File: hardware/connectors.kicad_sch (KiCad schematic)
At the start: 16 parts, among them J2 USB_C_Receptacle_USB2.0_16P, J7 Barrel_Jack_Switch

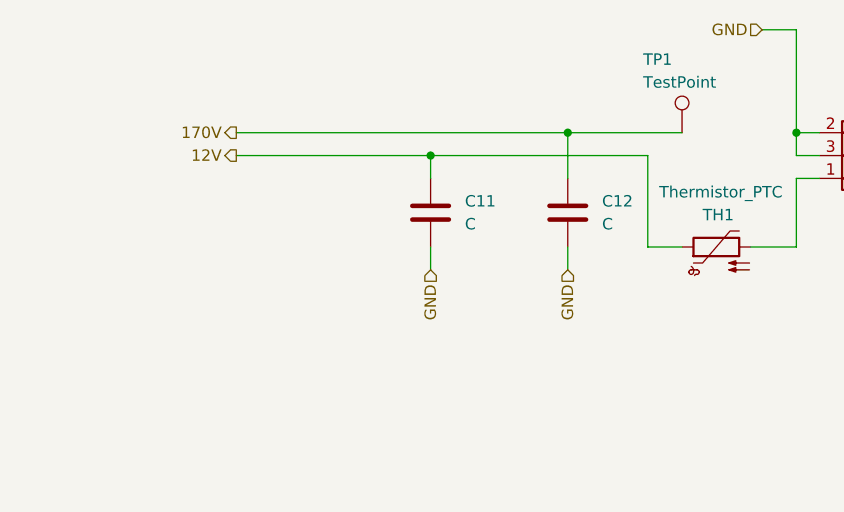
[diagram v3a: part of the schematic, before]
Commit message: Rework HT PSU placement.
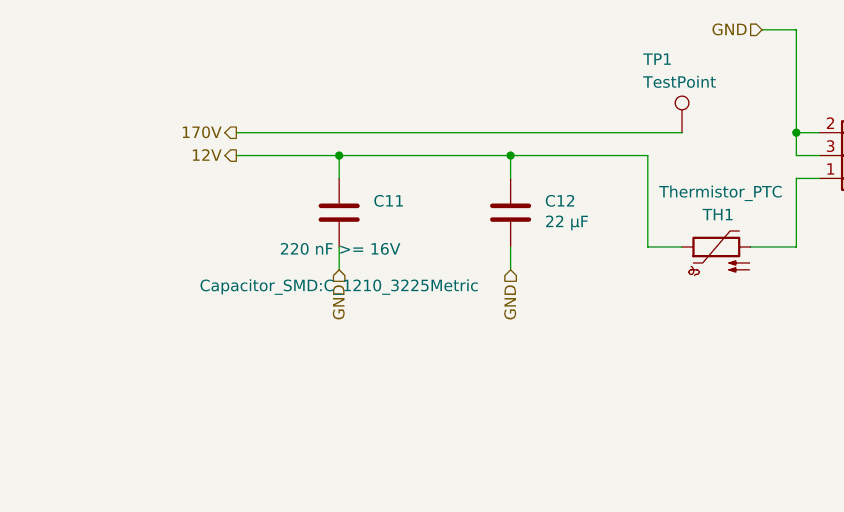
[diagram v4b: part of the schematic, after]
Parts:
- C11: value C -> 220 nF >= 16V; footprint Capacitor_SMD:C_1206_3216Metric -> Capacitor_SMD:C_1210_3225Metric
- C12: value C -> 22 µF; footprint Capacitor_THT:CP_Radial_D8.0mm_P3.50mm -> Capacitor_SMD:CP_Elec_6.3x5.4
- TP1: footprint TestPoint:TestPoint_Pad_D2.0mm -> TestPoint:TestPoint_Pad_D1.5mm
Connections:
- net 12V: now also C12.1
- net 170V: no longer C12.1
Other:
- moved on the sheet: C11
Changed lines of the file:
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@@
-	)
-	(junction
-		(at 189.23 38.1)
-		(diameter 0)
-		(color 0 0 0 0)
 	)
 	(junction
@@
 	)
 	(junction
-		(at 173.99 40.64)
+		(at 182.88 40.64)
 		(diameter 0)
 		(color 0 0 0 0)
 	)
-	(wire
-		(pts
-			(xy 173.99 43.18) (xy 173.99 40.64)
+	(junction
+		(at 163.83 40.64)
+		(diameter 0)
+		(color 0 0 0 0)
+	)
+	(wire
+		(pts
+			(xy 163.83 43.18) (xy 163.83 40.64)
 		)
 		(stroke
@@
 	(wire
 		(pts
+			(xy 182.88 50.8) (xy 182.88 53.34)
+		)
+		(stroke
+			(width 0)
+			(type default)
+		)
+	)
+	(wire
+		(pts
 			(xy 198.12 50.8) (xy 201.93 50.8)
 		)
@@
 	(wire
 		(pts
-			(xy 189.23 50.8) (xy 189.23 53.34)
-		)
-		(stroke
-			(width 0)
-			(type default)
-		)
-	)
-	(wire
-		(pts
 			(xy 105.41 52.07) (xy 111.76 52.07)
 		)
@@
 	(wire
 		(pts
+			(xy 182.88 43.18) (xy 182.88 40.64)
+		)
+		(stroke
+			(width 0)
+			(type default)
+		)
+	)
+	(wire
+		(pts
 			(xy 77.47 57.15) (xy 83.82 57.15)
 		)
@@
 	(wire
 		(pts
-			(xy 189.23 38.1) (xy 189.23 43.18)
+			(xy 182.88 40.64) (xy 198.12 40.64)
 		)
 		(stroke
@@
 	(wire
 		(pts
-			(xy 173.99 53.34) (xy 173.99 50.8)
-		)
-		(stroke
-			(width 0)
-			(type default)
-		)
-	)
-	(wire
-		(pts
 			(xy 60.96 82.55) (xy 60.96 96.52)
 		)
@@
 	(wire
 		(pts
-			(xy 189.23 38.1) (xy 201.93 38.1)
-		)
-		(stroke
-			(width 0)
-			(type default)
-		)
-	)
-	(wire
-		(pts
 			(xy 209.55 50.8) (xy 214.63 50.8)
 		)
@@
 	(wire
 		(pts
-			(xy 152.4 40.64) (xy 173.99 40.64)
-		)
-		(stroke
-			(width 0)
-			(type default)
-		)
-	)
-	(wire
-		(pts
-			(xy 152.4 38.1) (xy 189.23 38.1)
+			(xy 152.4 40.64) (xy 163.83 40.64)
+		)
+		(stroke
+			(width 0)
+			(type default)
+		)
+	)
+	(wire
+		(pts
+			(xy 152.4 38.1) (xy 201.93 38.1)
 		)
 		(stroke
@@
 	(wire
 		(pts
+			(xy 163.83 50.8) (xy 163.83 53.34)
+		)
+		(stroke
+			(width 0)
+			(type default)
+		)
+	)
+	(wire
+		(pts
 			(xy 76.2 74.93) (xy 78.74 74.93)
 		)
@@
 	(wire
 		(pts
-			(xy 173.99 40.64) (xy 198.12 40.64)
-		)
-		(stroke
-			(width 0)
-			(type default)
-		)
-	)
-	(wire
-		(pts
 			(xy 214.63 38.1) (xy 217.17 38.1)
 		)
@@
 		(pts
 			(xy 53.34 92.71) (xy 53.34 96.52)
+		)
+		(stroke
+			(width 0)
+			(type default)
+		)
+	)
+	(wire
+		(pts
+			(xy 163.83 40.64) (xy 182.88 40.64)
 		)
 		(stroke
@@
 		)
 	)
+	(hierarchical_label "GND"
+		(shape input)
+		(at 182.88 53.34 270)
+		(effects
+			(font
+				(size 1.27 1.27)
+			)
+			(justify right)
+		)
+	)
 	(hierarchical_label "D+"
 		(shape output)
@@
 	(hierarchical_label "GND"
 		(shape input)
-		(at 173.99 53.34 270)
-		(effects
-			(font
-				(size 1.27 1.27)
-			)
-			(justify right)
-		)
-	)
-	(hierarchical_label "GND"
-		(shape input)
-		(at 189.23 53.34 270)
+		(at 163.83 53.34 270)
 		(effects
 			(font
@@
 	(symbol
 		(lib_id "Device:C")
-		(at 173.99 46.99 0)
+		(at 182.88 46.99 0)
 		(unit 1)
 		(exclude_from_sim no)
@@
 		(on_board yes)
 		(dnp no)
-		(fields_autoplaced yes)
+		(property "Reference" "C12"
+			(at 186.69 45.7199 0)
+			(effects
+				(font
+					(size 1.27 1.27)
+				)
+				(justify left)
+			)
+		)
+		(property "Value" "22 µF"
+			(at 186.69 48.006 0)
+			(effects
+				(font
+					(size 1.27 1.27)
+				)
+				(justify left)
+			)
+		)
+		(property "Footprint" "Capacitor_SMD:CP_Elec_6.3x5.4"
+			(at 183.8452 50.8 0)
+			(effects
+				(font
+					(size 1.27 1.27)
+				)
+				(hide yes)
+			)
+		)
+		(property "Datasheet" "~"
+			(at 182.88 46.99 0)
+			(effects
+				(font
+					(size 1.27 1.27)
+				)
+				(hide yes)
+			)
+		)
+		(property "Description" "Unpolarized capacitor"
+			(at 182.88 46.99 0)
+			(effects
+				(font
+					(size 1.27 1.27)
+				)
+				(hide yes)
+			)
+		)
+		(pin "1"
+		)
+		(pin "2"
+		)
+		(instances
+			(project "nixie_clock"
+				(path "/90430e5f-7049-4de8-b92d-f897c4a89819/7e2fbc03-0d09-4c94-a49f-ff5156ee2f2b"
+					(reference "C12")
+					(unit 1)
+				)
+			)
+		)
+	)
+	(symbol
+		(lib_id "Device:C")
+		(at 163.83 46.99 0)
+		(unit 1)
+		(exclude_from_sim no)
+		(in_bom yes)
+		(on_board yes)
+		(dnp no)
 		(property "Reference" "C11"
-			(at 177.8 45.7199 0)
-			(effects
-				(font
-					(size 1.27 1.27)
-				)
-				(justify left)
-			)
-		)
-		(property "Value" "C"
-			(at 177.8 48.2599 0)
-			(effects
-				(font
-					(size 1.27 1.27)
-				)
-				(justify left)
-			)
-		)
-		(property "Footprint" "Capacitor_SMD:C_1206_3216Metric"
-			(at 174.9552 50.8 0)
-			(effects
-				(font
-					(size 1.27 1.27)
-				)
-				(hide yes)
+			(at 167.64 45.7199 0)
+			(effects
+				(font
+					(size 1.27 1.27)
+				)
+				(justify left)
+			)
+		)
+		(property "Value" "220 nF >= 16V"
+			(at 157.226 51.054 0)
+			(effects
+				(font
+					(size 1.27 1.27)
+				)
+				(justify left)
+			)
+		)
+		(property "Footprint" "Capacitor_SMD:C_1210_3225Metric"
+			(at 163.83 55.118 0)
+			(effects
+				(font
+					(size 1.27 1.27)
+				)
 			)
 		)
 		(property "Datasheet" "~"
-			(at 173.99 46.99 0)
+			(at 163.83 46.99 0)
 			(effects
 				(font
@@
 		)
 		(property "Description" "Unpolarized capacitor"
-			(at 173.99 46.99 0)
+			(at 163.83 46.99 0)
 			(effects
 				(font
@@
 			)
 		)
-		(property "Footprint" "TestPoint:TestPoint_Pad_D2.0mm"
+		(property "Footprint" "TestPoint:TestPoint_Pad_D1.5mm"
 			(at 207.01 38.1 0)
 			(effects
@@
 					(unit 1)
 				)
-			)
-		)
-	)
-	(symbol
-		(lib_id "Device:C")
-		(at 189.23 46.99 0)
-		(unit 1)
-		(exclude_from_sim no)
-		(in_bom yes)
-		(on_board yes)
-		(dnp no)
-		(fields_autoplaced yes)
-		(property "Reference" "C12"
-			(at 193.04 45.7199 0)
-			(effects
-				(font
-					(size 1.27 1.27)
-				)
-				(justify left)
-			)
-		)
-		(property "Value" "C"
-			(at 193.04 48.2599 0)
-			(effects
-				(font
-					(size 1.27 1.27)
-				)
-				(justify left)
-			)
-		)
-		(property "Footprint" "Capacitor_THT:CP_Radial_D8.0mm_P3.50mm"
-			(at 190.1952 50.8 0)
-			(effects
-				(font
-					(size 1.27 1.27)
-				)
-				(hide yes)
-			)
-		)
-		(property "Datasheet" "~"
-			(at 189.23 46.99 0)
-			(effects
-				(font
-					(size 1.27 1.27)
-				)
-				(hide yes)
-			)
-		)
-		(property "Description" "Unpolarized capacitor"
-			(at 189.23 46.99 0)
-			(effects
-				(font
-					(size 1.27 1.27)
-				)
-				(hide yes)
-			)
-		)
-		(pin "1"
-		)
-		(pin "2"
-		)
-		(instances
-			(project "qw"
-				(path "/90430e5f-7049-4de8-b92d-f897c4a89819/7e2fbc03-0d09-4c94-a49f-ff5156ee2f2b"
-					(reference "C12")
-					(unit 1)
-				)

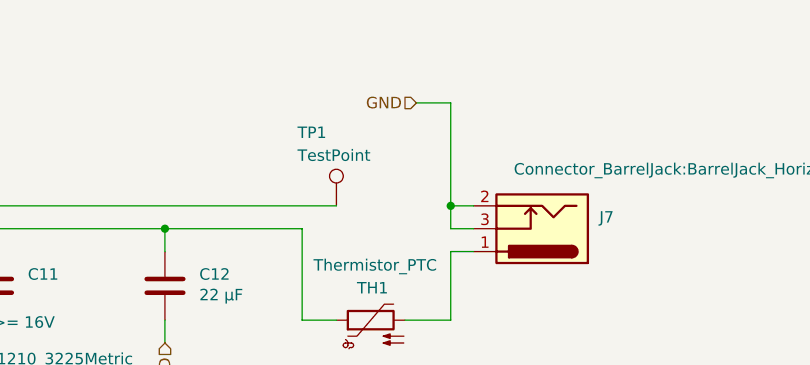
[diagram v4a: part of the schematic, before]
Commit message: Center USB-C connector on PCB. Add testpoints.
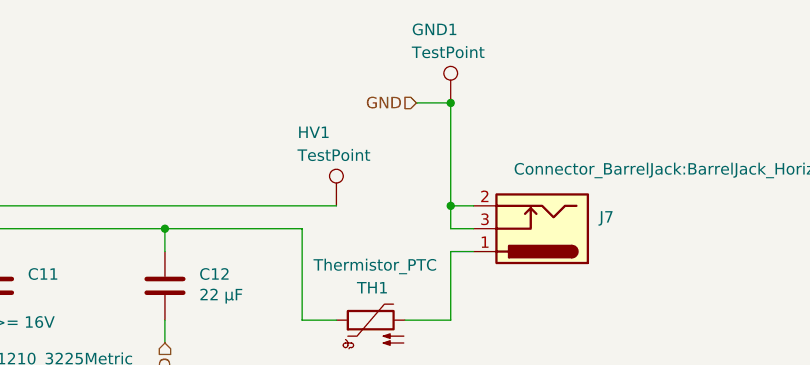
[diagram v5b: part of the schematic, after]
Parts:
- added GND1: TestPoint, TestPoint:TestPoint_Pad_D1.5mm, symbol Connector:TestPoint
- renumbered TP1 to HV1
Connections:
- net GND: now also GND1.1
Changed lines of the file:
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@@
+		(color 0 0 0 0)
+	)
+	(junction
+		(at 214.63 26.67)
+		(diameter 0)
 		(color 0 0 0 0)
 	)
@@
 		(on_board yes)
 		(dnp no)
-		(property "Reference" "TP1"
+		(property "Reference" "HV1"
 			(at 197.612 29.972 0)
 			(effects
@@
 			(project ""
 				(path "/90430e5f-7049-4de8-b92d-f897c4a89819/7e2fbc03-0d09-4c94-a49f-ff5156ee2f2b"
-					(reference "TP1")
+					(reference "HV1")
 					(unit 1)
 				)
@@
 					(unit 1)
 				)
+			)
+		)
+	)
+	(symbol
+		(lib_id "Connector:TestPoint")
+		(at 214.63 26.67 0)
+		(unit 1)
+		(exclude_from_sim no)
+		(in_bom yes)
+		(on_board yes)
+		(dnp no)
+		(property "Reference" "GND1"
+			(at 210.312 18.542 0)
+			(effects
+				(font
+					(size 1.27 1.27)
+				)
+				(justify left)
+			)
+		)
+		(property "Value" "TestPoint"
+			(at 210.312 21.082 0)
+			(effects
+				(font
+					(size 1.27 1.27)
+				)
+				(justify left)
+			)
+		)
+		(property "Footprint" "TestPoint:TestPoint_Pad_D1.5mm"
+			(at 219.71 26.67 0)
+			(effects
+				(font
+					(size 1.27 1.27)
+				)
+				(hide yes)
+			)
+		)
+		(property "Datasheet" "~"
+			(at 219.71 26.67 0)
+			(effects
+				(font
+					(size 1.27 1.27)
+				)
+				(hide yes)
+			)
+		)
+		(property "Description" "test point"
+			(at 214.63 26.67 0)
+			(effects
+				(font
+					(size 1.27 1.27)
+				)
+				(hide yes)
+			)
+		)
+		(pin "1"
+		)
+		(instances
+			(project "nixie_clock"
+				(path "/90430e5f-7049-4de8-b92d-f897c4a89819/7e2fbc03-0d09-4c94-a49f-ff5156ee2f2b"
+					(reference "GND1")
+					(unit 1)
+				)

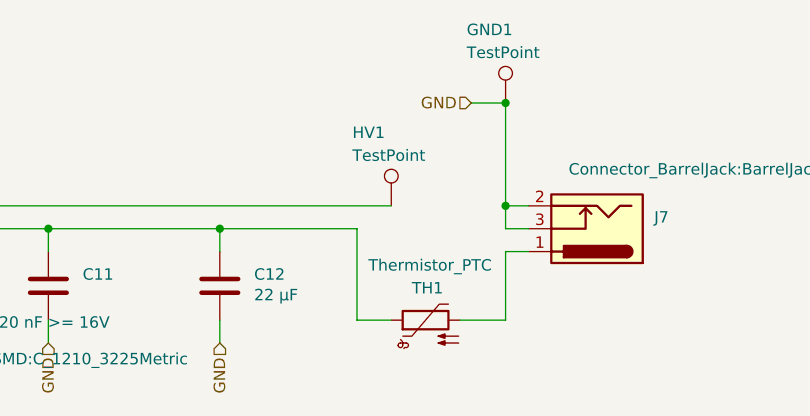
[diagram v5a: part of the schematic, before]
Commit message: Remove HV capacitor for Nixies. Add more LCSC references.
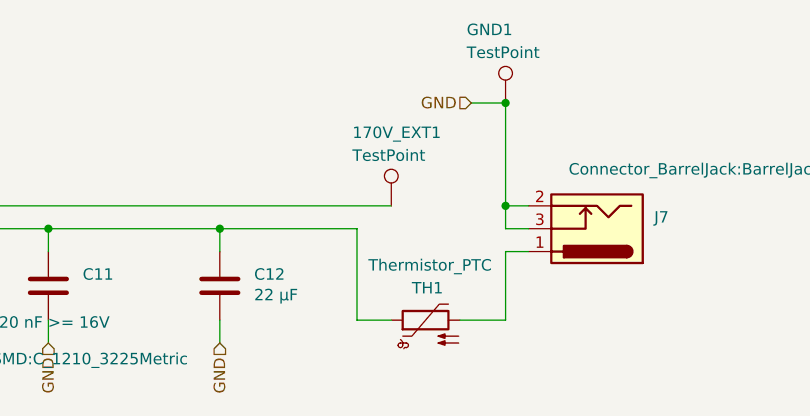
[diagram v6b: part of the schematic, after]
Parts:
- removed HV1: TestPoint, TestPoint:TestPoint_Pad_D1.5mm, symbol Connector:TestPoint
- added 170V_EXT1: TestPoint, TestPoint:TestPoint_Pad_D1.5mm, symbol Connector:TestPoint
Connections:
- net 170V: now also 170V_EXT1.1

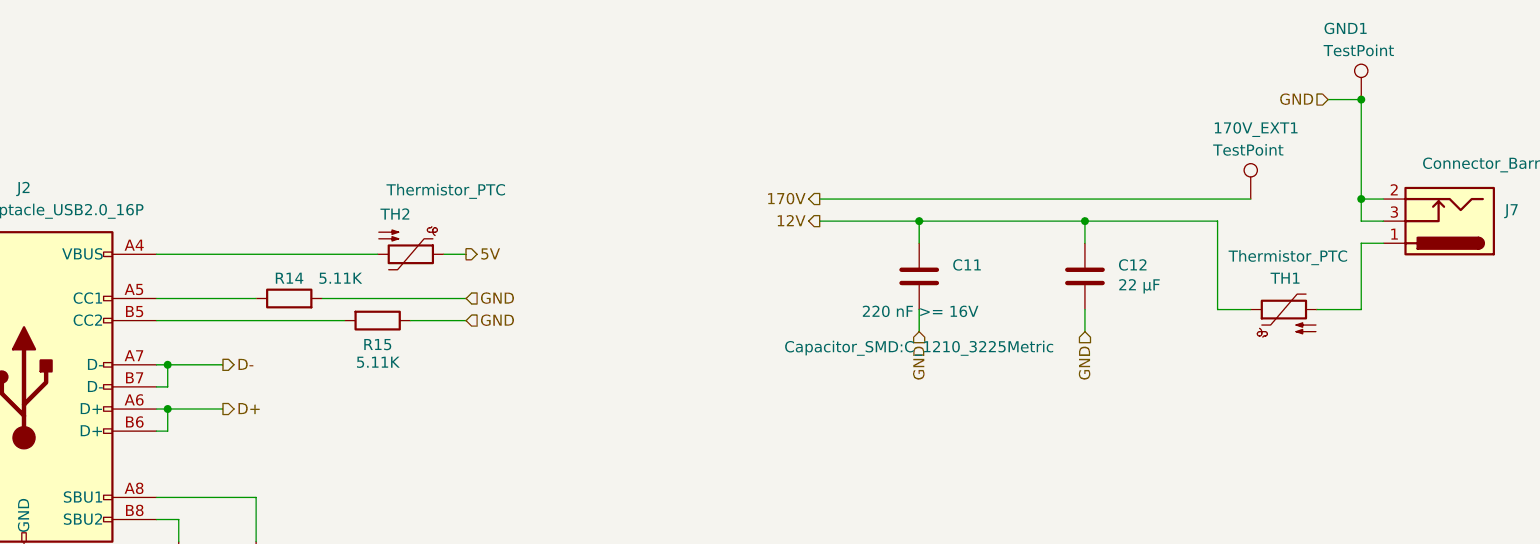
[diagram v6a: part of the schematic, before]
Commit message: Limitate inrush current (decoupling capacitors after PTCs). Add decoupling capacitors for VUSB.
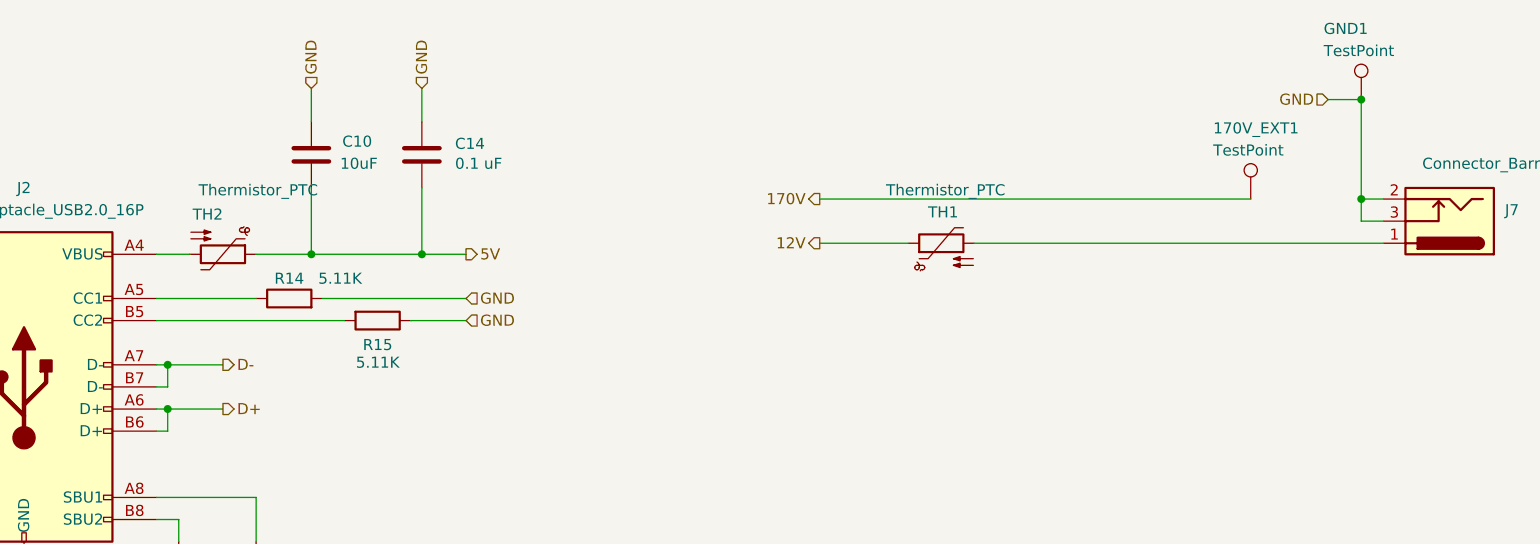
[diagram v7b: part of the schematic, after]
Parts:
- removed C11: 220 nF >= 16V, Capacitor_SMD:C_1210_3225Metric, symbol Device:C
- removed C12: 22 µF, Capacitor_SMD:CP_Elec_6.3x5.4, symbol Device:C
- added C10: 10uF, Capacitor_SMD:C_1206_3216Metric, symbol Device:C
- added C14: 0.1 uF, Capacitor_SMD:C_0805_2012Metric, symbol Device:C
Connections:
- net 5V: now also C10.2, C14.2
- net GND: now also C10.1, C14.1
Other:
- moved on the sheet: TH1, TH2
